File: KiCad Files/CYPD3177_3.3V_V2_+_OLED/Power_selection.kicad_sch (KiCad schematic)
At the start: 23 parts, among them IC2 TPS16630RGER, IC3 TPS22992SRXNR, U1 TPS2117DRL

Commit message: changed pcb
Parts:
- renumbered C31 to C16, C28 to C17, C27 to C18, C25 to C19, C26 to C20, C30 to C21, C29 to C22, D4 to D7, IC2 to IC1, IC3 to IC2, R16 to R21, R17 to R22, R19 to R23, R23 to R24, R35 to R25, R21 to R26, R22 to R27, R27 to R28, R15 to R29, R24 to R30, R26 to R31, U1 to U8

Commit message: schematics done
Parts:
- added R34: 10k, Resistor_SMD:R_0402_1005Metric, symbol Device:R
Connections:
- net +5V: now also IC1.15 (N.C_3), IC1.19 (N.C_4), IC1.20 (N.C_5), IC1.21 (N.C_6), IC1.22 (N.C_7), IC1.23 (N.C_8), IC1.24 (N.C_9), IC1.3 (N.C_1), IC1.4 (N.C_2), R34.1
- net PGOOD: now reaches IC1.16 (PGOOD)
- net PGOOD: now also R34.2
- net Rail_2 renamed Rail_2_IN
- no-connect marks 1 -> 0
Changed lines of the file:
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@@
+	)
+	(junction
+		(at 71.12 104.14)
+		(diameter 0)
+		(color 0 0 0 0)
 	)
 	(junction
@@
 		(color 0 0 0 0)
 	)
-	(no_connect
-		(at 71.12 104.14)
-	)
 	(wire
 		(pts
@@
 		(pts
 			(xy 115.57 50.8) (xy 118.11 50.8)
+		)
+		(stroke
+			(width 0)
+			(type default)
+		)
+	)
+	(wire
+		(pts
+			(xy 71.12 95.25) (xy 71.12 104.14)
 		)
 		(stroke
@@
 		)
 	)
-	(hierarchical_label "Rail_2"
+	(hierarchical_label "Rail_2_IN"
 		(shape output)
-		(at 116.84 119.38 0)
+		(at 245.11 127 0)
 		(effects
 			(font
@@
 		)
 	)
-	(hierarchical_label "Rail_2"
+	(hierarchical_label "PGOOD"
 		(shape output)
-		(at 245.11 127 0)
+		(at 71.12 95.25 90)
 		(effects
 			(font
@@
 		(shape input)
 		(at 209.55 102.87 90)
+		(effects
+			(font
+				(size 1.27 1.27)
+			)
+			(justify left)
+		)
+	)
+	(hierarchical_label "Rail_2_IN"
+		(shape output)
+		(at 116.84 119.38 0)
 		(effects
 			(font
@@
 	)
 	(symbol
+		(lib_id "power:+5V")
+		(at 78.74 104.14 270)
+		(unit 1)
+		(exclude_from_sim no)
+		(in_bom yes)
+		(on_board yes)
+		(dnp no)
+		(fields_autoplaced yes)
+		(property "Reference" "#PWR078"
+			(at 74.93 104.14 0)
+			(effects
+				(font
+					(size 1.27 1.27)
+				)
+				(hide yes)
+			)
+		)
+		(property "Value" "+5V"
+			(at 82.55 104.1399 90)
+			(effects
+				(font
+					(size 1.27 1.27)
+				)
+				(justify left)
+			)
+		)
+		(property "Footprint" ""
+			(at 78.74 104.14 0)
+			(effects
+				(font
+					(size 1.27 1.27)
+				)
+				(hide yes)
+			)
+		)
+		(property "Datasheet" ""
+			(at 78.74 104.14 0)
+			(effects
+				(font
+					(size 1.27 1.27)
+				)
+				(hide yes)
+			)
+		)
+		(property "Description" "Power symbol creates a global label with name \"+5V\""
+			(at 78.74 104.14 0)
+			(effects
+				(font
+					(size 1.27 1.27)
+				)
+				(hide yes)
+			)
+		)
+		(pin "1"
+		)
+		(instances
+			(project "CYPD3177_3.3V_V2_+_OLED"
+				(path "/a370047b-ebc6-4236-825e-9462ba7e4392/ed97b83e-5e05-4a40-92ea-fb87b568f4be"
+					(reference "#PWR078")
+					(unit 1)
+				)
+			)
+		)
+	)
+	(symbol
 		(lib_id "power:GND")
 		(at 111.76 130.81 0)
@@
 					(unit 1)
 				)
+			)
+		)
+	)
+	(symbol
+		(lib_id "Device:R")
+		(at 74.93 104.14 270)
+		(unit 1)
+		(exclude_from_sim no)
+		(in_bom yes)
+		(on_board yes)
+		(dnp no)
+		(property "Reference" "R34"
+			(at 75.692 98.552 0)
+			(effects
+				(font
+					(size 1.27 1.27)
+				)
+				(justify left)
+			)
+		)
+		(property "Value" "10k"
+			(at 72.898 98.806 0)
+			(effects
+				(font
+					(size 1.27 1.27)
+				)
+				(justify left)
+			)
+		)
+		(property "Footprint" "Resistor_SMD:R_0402_1005Metric"
+			(at 74.93 102.362 90)
+			(effects
+				(font
+					(size 1.27 1.27)
+				)
+				(hide yes)
+			)
+		)
+		(property "Datasheet" "~"
+			(at 74.93 104.14 0)
+			(effects
+				(font
+					(size 1.27 1.27)
+				)
+				(hide yes)
+			)
+		)
+		(property "Description" "Resistor"
+			(at 74.93 104.14 0)
+			(effects
+				(font
+					(size 1.27 1.27)
+				)
+				(hide yes)
+			)
+		)
+		(property "LCSC" "C25744"
+			(at 74.93 104.14 0)
+			(effects
+				(font
+					(size 1.27 1.27)
+				)
+				(hide yes)
+			)
+		)
+		(pin "2"
+		)
+		(pin "1"
+		)
+		(instances
+			(project "CYPD3177_3.3V_V2_+_OLED"
+				(path "/a370047b-ebc6-4236-825e-9462ba7e4392/ed97b83e-5e05-4a40-92ea-fb87b568f4be"
+					(reference "R34")
+					(unit 1)
+				)

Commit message: major cahnges do desing, now think final design before designing pcb
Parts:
- C16, C17, C18, C19, C20, C21, C22: footprint Capacitor_SMD:C_1206_3216Metric -> Capacitor_SMD:C_0402_1005Metric_Pad0.74x0.62mm_HandSolder
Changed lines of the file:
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@@
 			)
 		)
-		(property "Footprint" "Capacitor_SMD:C_1206_3216Metric"
+		(property "Footprint" "Capacitor_SMD:C_0402_1005Metric_Pad0.74x0.62mm_HandSolder"
 			(at 51.1048 111.76 0)
 			(effects
@@
 			)
 		)
-		(property "Footprint" "Capacitor_SMD:C_1206_3216Metric"
+		(property "Footprint" "Capacitor_SMD:C_0402_1005Metric_Pad0.74x0.62mm_HandSolder"
 			(at 192.0748 133.35 0)
 			(effects
@@
 			)
 		)
-		(property "Footprint" "Capacitor_SMD:C_1206_3216Metric"
+		(property "Footprint" "Capacitor_SMD:C_0402_1005Metric_Pad0.74x0.62mm_HandSolder"
 			(at 158.4452 48.26 0)
 			(effects
@@
 			)
 		)
-		(property "Footprint" "Capacitor_SMD:C_1206_3216Metric"
+		(property "Footprint" "Capacitor_SMD:C_0402_1005Metric_Pad0.74x0.62mm_HandSolder"
 			(at 85.3948 144.78 0)
 			(effects
@@
 			)
 		)
-		(property "Footprint" "Capacitor_SMD:C_1206_3216Metric"
+		(property "Footprint" "Capacitor_SMD:C_0402_1005Metric_Pad0.74x0.62mm_HandSolder"
 			(at 207.9752 156.21 0)
 			(effects
@@
 			)
 		)
-		(property "Footprint" "Capacitor_SMD:C_1206_3216Metric"
+		(property "Footprint" "Capacitor_SMD:C_0402_1005Metric_Pad0.74x0.62mm_HandSolder"
 			(at 130.5052 48.26 0)
 			(effects
@@
 			)
 		)
-		(property "Footprint" "Capacitor_SMD:C_1206_3216Metric"
+		(property "Footprint" "Capacitor_SMD:C_0402_1005Metric_Pad0.74x0.62mm_HandSolder"
 			(at 94.2848 111.76 0)
 			(effects

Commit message: changes
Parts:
- C16, C17, C18, C19, C20, C21, C22: footprint Capacitor_SMD:C_0402_1005Metric_Pad0.74x0.62mm_HandSolder -> Capacitor_SMD:C_0402_1005Metric
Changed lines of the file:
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@@
 			)
 		)
-		(property "Footprint" "Capacitor_SMD:C_0402_1005Metric_Pad0.74x0.62mm_HandSolder"
+		(property "Footprint" "Capacitor_SMD:C_0402_1005Metric"
 			(at 51.1048 111.76 0)
 			(effects
@@
 			)
 		)
-		(property "Footprint" "Capacitor_SMD:C_0402_1005Metric_Pad0.74x0.62mm_HandSolder"
+		(property "Footprint" "Capacitor_SMD:C_0402_1005Metric"
 			(at 192.0748 133.35 0)
 			(effects
@@
 			)
 		)
-		(property "Footprint" "Capacitor_SMD:C_0402_1005Metric_Pad0.74x0.62mm_HandSolder"
+		(property "Footprint" "Capacitor_SMD:C_0402_1005Metric"
 			(at 158.4452 48.26 0)
 			(effects
@@
 			)
 		)
-		(property "Footprint" "Capacitor_SMD:C_0402_1005Metric_Pad0.74x0.62mm_HandSolder"
+		(property "Footprint" "Capacitor_SMD:C_0402_1005Metric"
 			(at 85.3948 144.78 0)
 			(effects
@@
 			)
 		)
-		(property "Footprint" "Capacitor_SMD:C_0402_1005Metric_Pad0.74x0.62mm_HandSolder"
+		(property "Footprint" "Capacitor_SMD:C_0402_1005Metric"
 			(at 207.9752 156.21 0)
 			(effects
@@
 			)
 		)
-		(property "Footprint" "Capacitor_SMD:C_0402_1005Metric_Pad0.74x0.62mm_HandSolder"
+		(property "Footprint" "Capacitor_SMD:C_0402_1005Metric"
 			(at 130.5052 48.26 0)
 			(effects
@@
 			)
 		)
-		(property "Footprint" "Capacitor_SMD:C_0402_1005Metric_Pad0.74x0.62mm_HandSolder"
+		(property "Footprint" "Capacitor_SMD:C_0402_1005Metric"
 			(at 94.2848 111.76 0)
 			(effects

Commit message: changes
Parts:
- removed D6, D7: PMEG6020ER, Diode_SMD:D_SOD-123F, symbol Diode:PMEG6020ER

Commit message: changes
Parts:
- renumbered C17 to C8, R26 to R4
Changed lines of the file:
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@@
 		(on_board yes)
 		(dnp no)
-		(property "Reference" "C17"
+		(property "Reference" "C8"
 			(at 83.312 150.622 0)
 			(effects
@@
 			(project "CYPD3177_3.3V_V2_+_OLED"
 				(path "/a370047b-ebc6-4236-825e-9462ba7e4392/ed97b83e-5e05-4a40-92ea-fb87b568f4be"
-					(reference "C17")
+					(reference "C8")
 					(unit 1)
 				)
@@
 		(on_board yes)
 		(dnp no)
-		(property "Reference" "R26"
+		(property "Reference" "R4"
 			(at 100.33 150.622 0)
 			(effects
@@
 			(project "CYPD3177_3.3V_V2_+_OLED"
 				(path "/a370047b-ebc6-4236-825e-9462ba7e4392/ed97b83e-5e05-4a40-92ea-fb87b568f4be"
-					(reference "R26")
-					(unit 1)
-				)
+					(reference "R4")
+					(unit 1)
+				)

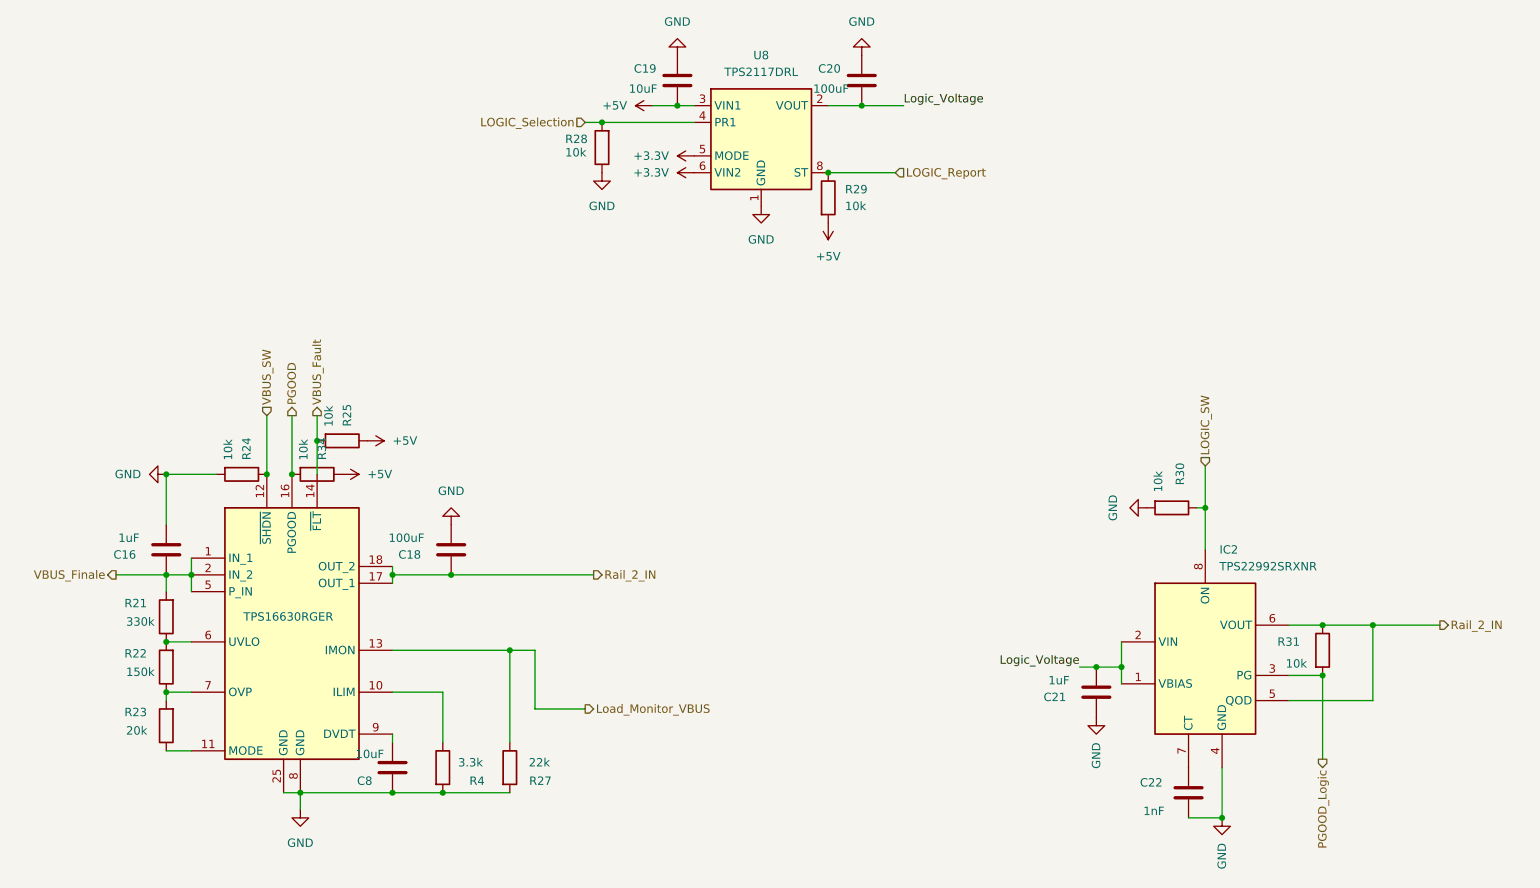
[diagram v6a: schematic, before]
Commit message: finshed pcb, assigning part numbers
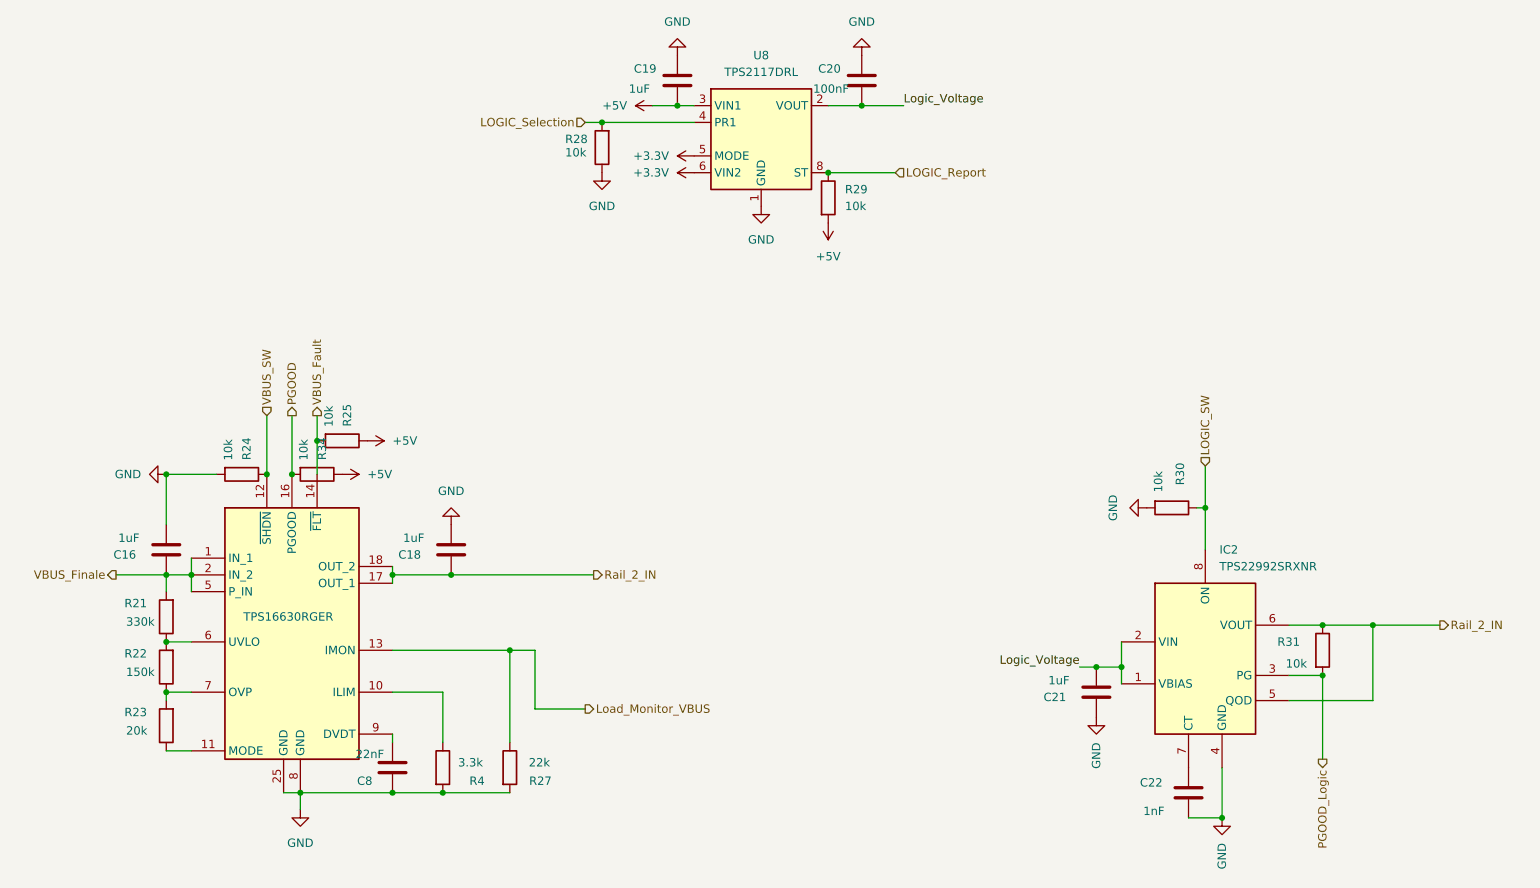
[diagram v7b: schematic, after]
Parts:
- C16: footprint Capacitor_SMD:C_0402_1005Metric -> Capacitor_SMD:C_0603_1608Metric
- C18: value 100uF -> 1uF; footprint Capacitor_SMD:C_0402_1005Metric -> Capacitor_SMD:C_0603_1608Metric
- C19: value 10uF -> 1uF
- C20: value 100uF -> 100nF
- C8: value 10uF -> 22nF
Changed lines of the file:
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@@
 			)
 		)
-		(property "Footprint" "Capacitor_SMD:C_0402_1005Metric"
+		(property "Footprint" "Capacitor_SMD:C_0603_1608Metric"
 			(at 51.1048 111.76 0)
 			(effects
@@
 			)
 		)
-		(property "Value" "100uF"
+		(property "Value" "100nF"
 			(at 150.114 45.72 0)
 			(effects
@@
 			)
 		)
-		(property "Value" "10uF"
+		(property "Value" "22nF"
 			(at 85.09 146.558 0)
 			(effects
@@
 			)
 		)
-		(property "Value" "10uF"
+		(property "Value" "1uF"
 			(at 122.174 45.72 0)
 			(effects
@@
 			)
 		)
-		(property "Value" "100uF"
+		(property "Value" "1uF"
 			(at 91.186 113.7919 0)
 			(effects
@@
 			)
 		)
-		(property "Footprint" "Capacitor_SMD:C_0402_1005Metric"
+		(property "Footprint" "Capacitor_SMD:C_0603_1608Metric"
 			(at 94.2848 111.76 0)
 			(effects

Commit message: changes
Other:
- title: (none) -> USB PD PPS for breadboards
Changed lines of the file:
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@@
 	(generator_version "9.0")
 	(paper "A4")
+	(title_block
+		(title "USB PD PPS for breadboards")
+		(date "2025-05-01")
+		(rev "V1")
+		(comment 1 "Licensed under CC BY-NC-SA 4.0 (c) 2025 Shinui")
+	)
 	(junction
 		(at 129.54 48.26)
